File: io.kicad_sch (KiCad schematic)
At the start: 5 parts, among them SW1 Reset, U3 6821

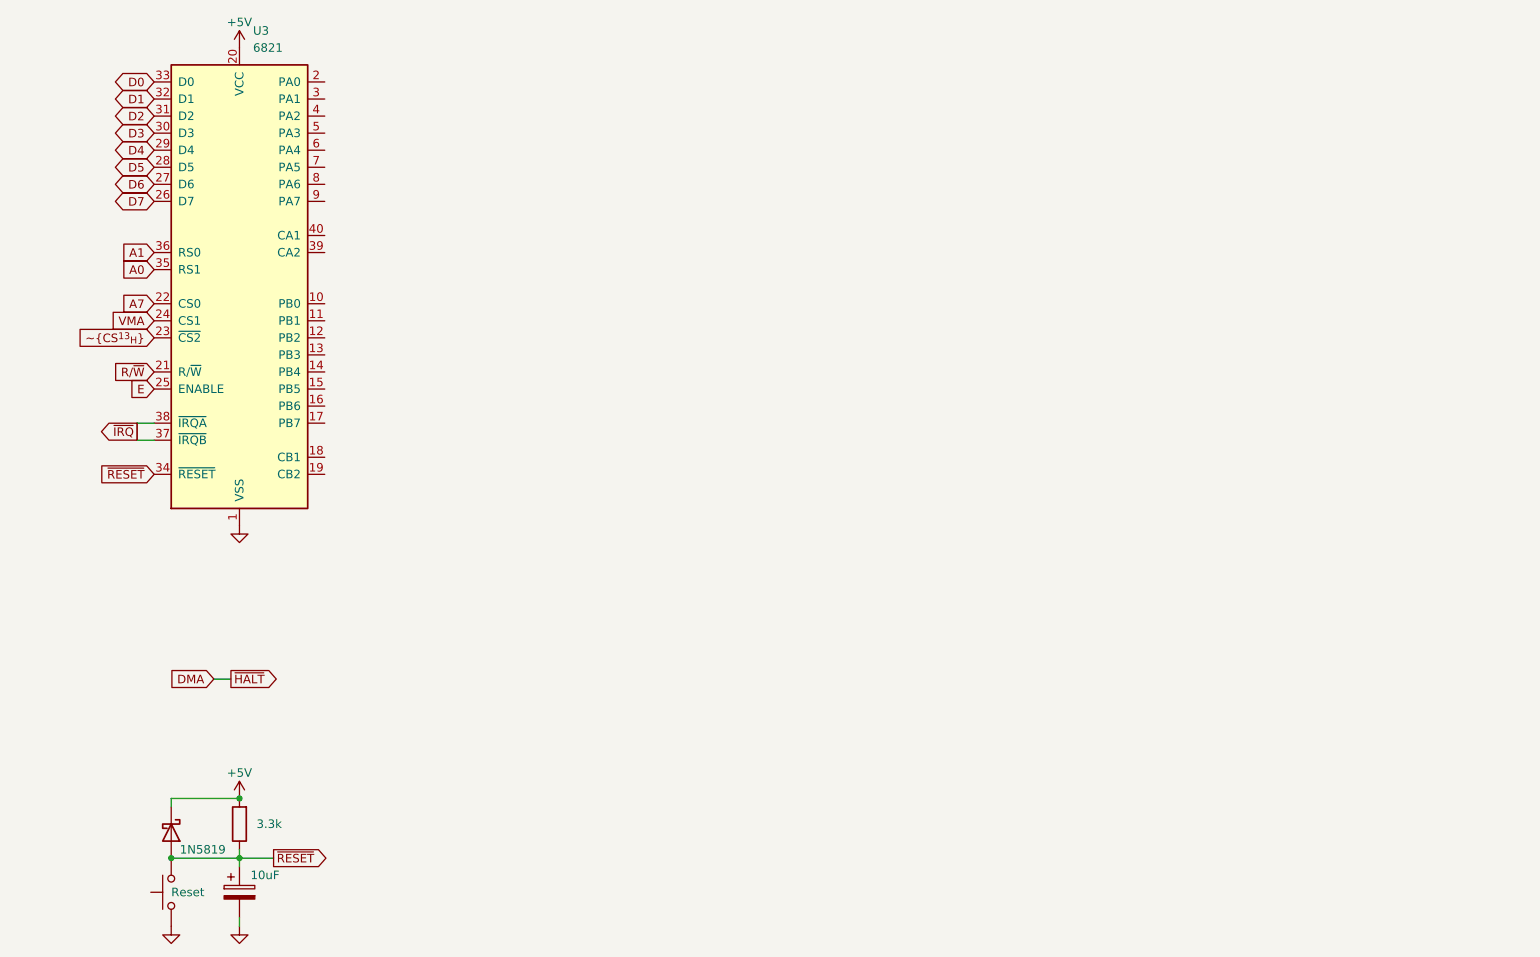
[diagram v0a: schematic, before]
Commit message: add uart
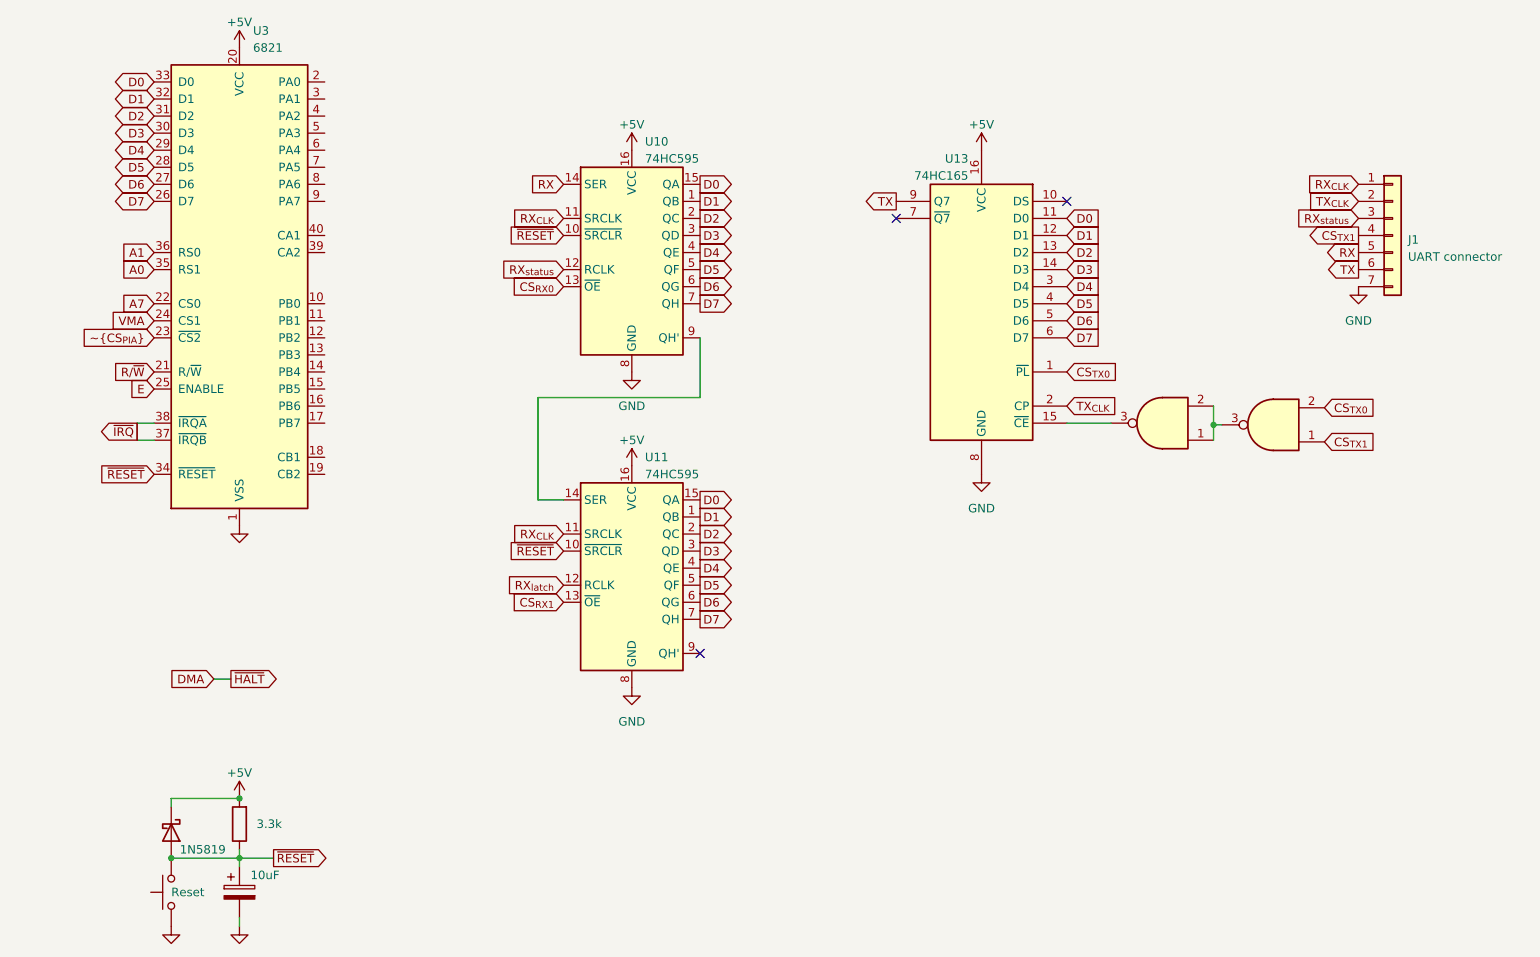
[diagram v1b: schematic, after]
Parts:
- added J1: UART connector, symbol Connector_Generic:Conn_01x07
- added U10, U11: 74HC595, Package_DIP:DIP-16_W7.62mm_Socket, symbol 74xx:74HC595
- added U13: 74HC165, symbol 74xx:74HC165
- added U14, U15: 74HC00, symbol 74xx:74HC00
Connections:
- net +5V: now also U10.16 (VCC), U11.16 (VCC), U13.16 (VCC)
- net D0: now also U10.15 (QA), U11.15 (QA), U13.11 (D0)
- net D1: now also U10.1 (QB), U11.1 (QB), U13.12 (D1)
- net D2: now also U10.2 (QC), U11.2 (QC), U13.13 (D2)
- net D3: now also U10.3 (QD), U11.3 (QD), U13.14 (D3)
- net D4: now also U10.4 (QE), U11.4 (QE), U13.3 (D4)
- net D5: now also U10.5 (QF), U11.5 (QF), U13.4 (D5)
- net D6: now also U10.6 (QG), U11.6 (QG), U13.5 (D6)
- net D7: now also U10.7 (QH), U11.7 (QH), U13.6 (D7)
- net GND: now also J1.7 (Pin_7), U10.8 (GND), U11.8 (GND), U13.8 (GND)
- net ~{RESET}: now also U10.10 (~{SRCLR}), U11.10 (~{SRCLR})
- net ~{CS^{13}_{H}} renamed ~{CS_{PIA}}
- new net: U10.9 (QH'), U11.14 (SER)
- new net: U13.15 (~{CE}), U14.3
- new net: U14.1, U14.2, U15.3
- new net CS_{RX0}: U10.13 (~{OE})
- new net CS_{RX1}: U11.13 (~{OE})
- new net CS_{TX0}: U13.1 (~{PL}), U15.2
- new net CS_{TX1}: J1.4 (Pin_4), U15.1
- new net RX: J1.5 (Pin_5), U10.14 (SER)
- new net RX_{CLK}: J1.1 (Pin_1), U10.11 (SRCLK), U11.11 (SRCLK)
- new net RX_{latch}: U11.12 (RCLK)
- new net RX_{status}: J1.3 (Pin_3), U10.12 (RCLK)
- new net TX: J1.6 (Pin_6), U13.9 (Q7)
- new net TX_{CLK}: J1.2 (Pin_2), U13.2 (CP)
- no-connect marks 0 -> 3
